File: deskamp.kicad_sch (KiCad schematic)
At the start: 34 parts, among them J1 Input 01, J10 Input Select, J2 Input 02, J3 Preamp Out, J5 LFE, J6 Mute, J7 Sleep, J8 Motor, J9 Power, K1 TQ2-12V, K2 TQ2-12V, K3 TQ2-12V, K4 TQ2-12V, Q1 PN2222A, Q2 PN2222A, Q3 PN2222A, Q4 PN2222A, U1 esp32-wemos-d1-mini, U2 L9110, U3 TSR_1-2433

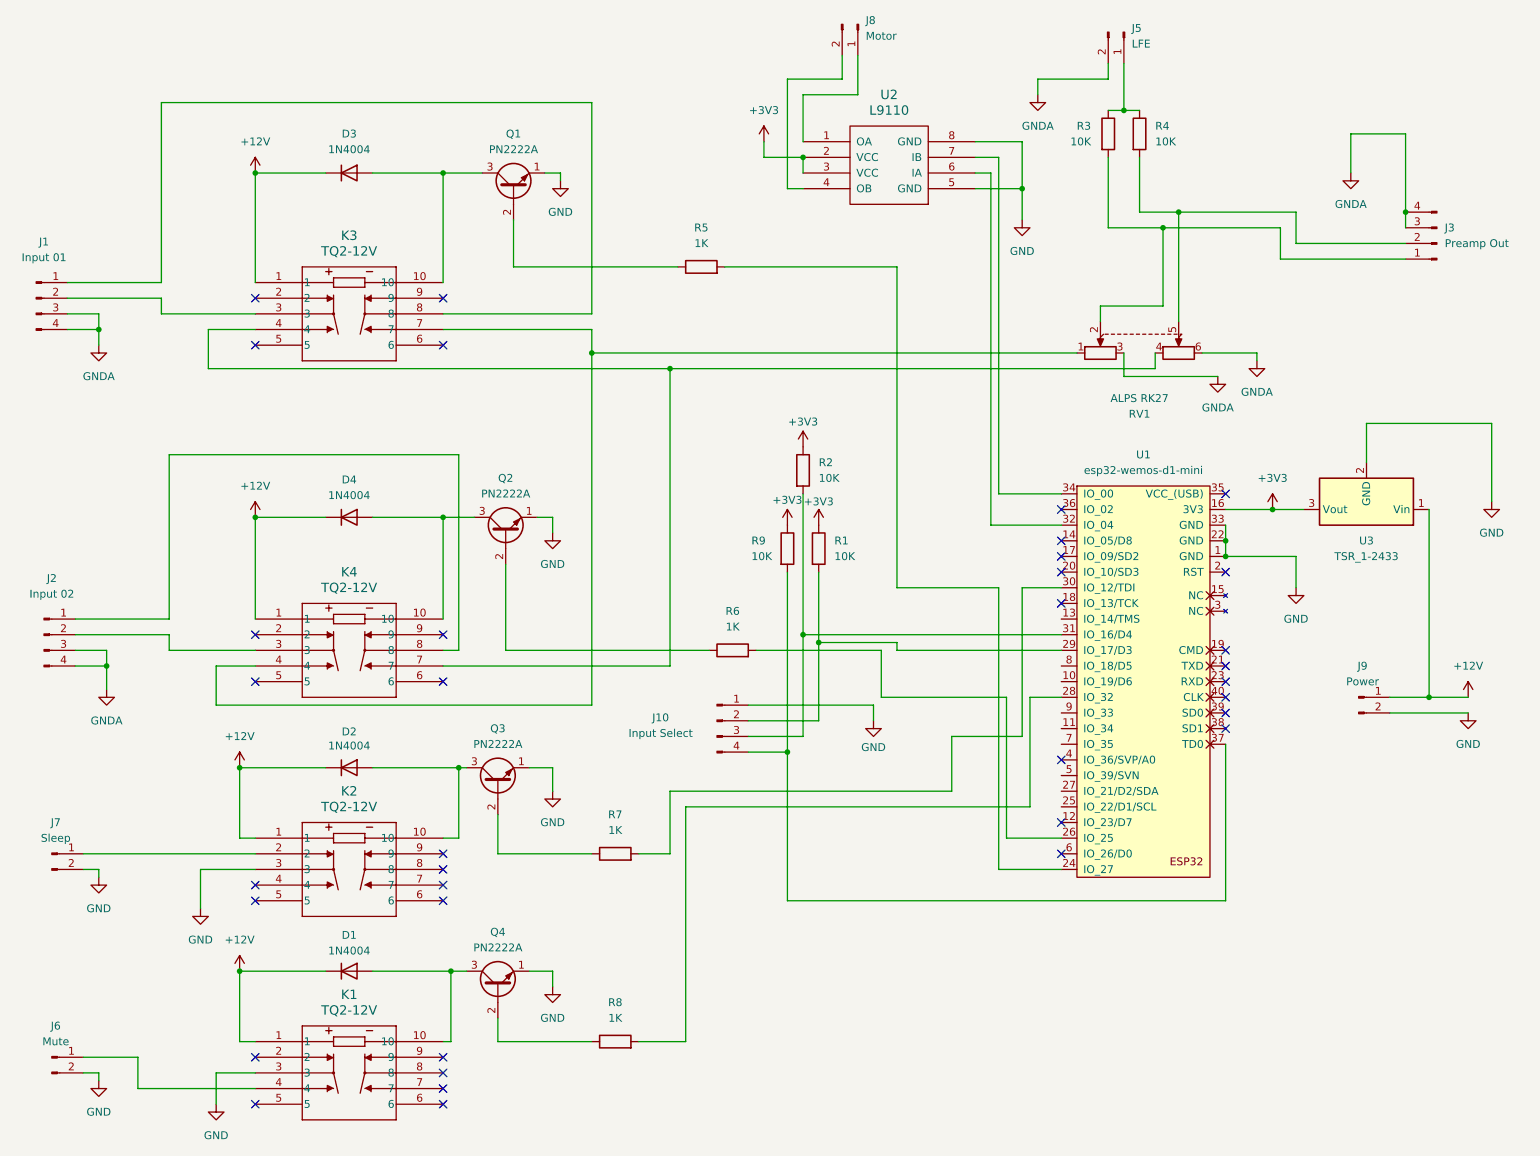
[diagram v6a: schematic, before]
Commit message: Start afresh with layout
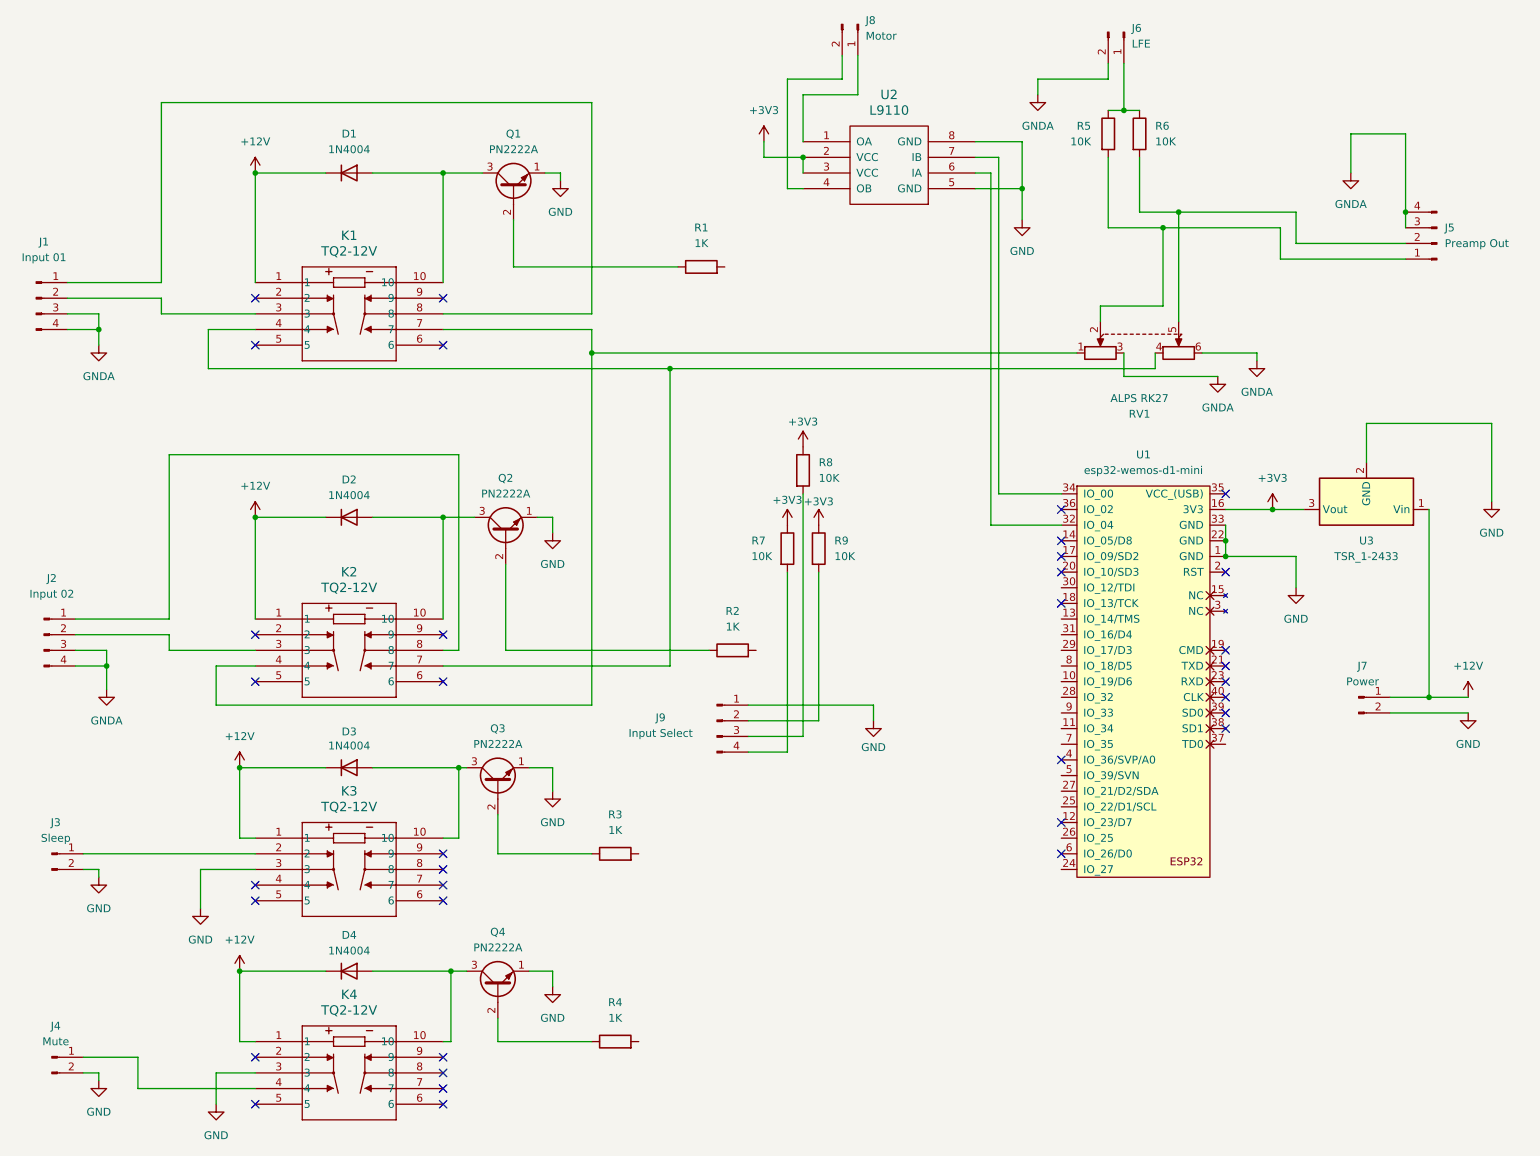
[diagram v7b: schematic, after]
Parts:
- renumbered D3 to D1, D4 to D2, D2 to D3, D1 to D4, J7 to J3, J6 to J4, J3 to J5, J5 to J6, J9 to J7, J10 to J9, K3 to K1, K4 to K2, K2 to K3, K1 to K4, R5 to R1, R6 to R2, R7 to R3, R8 to R4, R3 to R5, R4 to R6, R9 to R7, R2 to R8, R1 to R9
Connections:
- net at R4.2: no longer U1.28 (IO_32)
- net at J9.2 (Pin_2), R9.2: no longer U1.29 (IO_17/D3)
- net at R2.2: no longer U1.26 (IO_25)
- net at J9.3 (Pin_3), R8.2: no longer U1.31 (IO_16/D4)
- net at J9.4 (Pin_4), R7.2: no longer U1.37 (TD0)
- net at R1.2: no longer U1.24 (IO_27)
- net at U1.30 (IO_12/TDI): no longer R3.2

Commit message: Board layout
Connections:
- net Motor_P: now reaches U1.32 (IO_04), U2.6 (IA)
- net Motor_N: now reaches U1.34 (IO_00), U2.7 (IB)
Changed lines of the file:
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@@
-	(wire
-		(pts
-			(xy 193.04 92.71) (xy 182.88 92.71)
-		)
-		(stroke
-			(width 0)
-			(type default)
-		)
-	)
 	(wire
 		(pts
@@
 	(wire
 		(pts
+			(xy 182.88 38.1) (xy 182.88 92.71)
+		)
+		(stroke
+			(width 0)
+			(type default)
+		)
+	)
+	(wire
+		(pts
 			(xy 193.04 97.79) (xy 181.61 97.79)
 		)
@@
 	(wire
 		(pts
-			(xy 182.88 92.71) (xy 182.88 38.1)
-		)
-		(stroke
-			(width 0)
-			(type default)
-		)
-	)
-	(wire
-		(pts
 			(xy 31.75 58.42) (xy 46.99 58.42)
 		)
@@
 	(wire
 		(pts
+			(xy 182.88 92.71) (xy 193.04 92.71)
+		)
+		(stroke
+			(width 0)
+			(type default)
+		)
+	)
+	(wire
+		(pts
 			(xy 219.71 100.33) (xy 219.71 102.87)
 		)
@@
 		)
 	)
+	(label "Motor_N"
+		(at 184.15 92.71 0)
+		(effects
+			(font
+				(size 1.27 1.27)
+			)
+			(justify left bottom)
+		)
+	)
+	(label "Motor_P"
+		(at 182.88 97.79 0)
+		(effects
+			(font
+				(size 1.27 1.27)
+			)
+			(justify left bottom)
+		)
+	)
